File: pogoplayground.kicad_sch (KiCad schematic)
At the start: 48 parts, among them J2 Conn_01x20, J3 Conn_ARM_JTAG_SWD_10, J4 Conn_ARM_JTAG_SWD_10, J5 Conn_01x08, J6 Conn_01x30, J7 Conn_02x04_Odd_Even, J8 Conn_01x24, J9 Conn_01x02

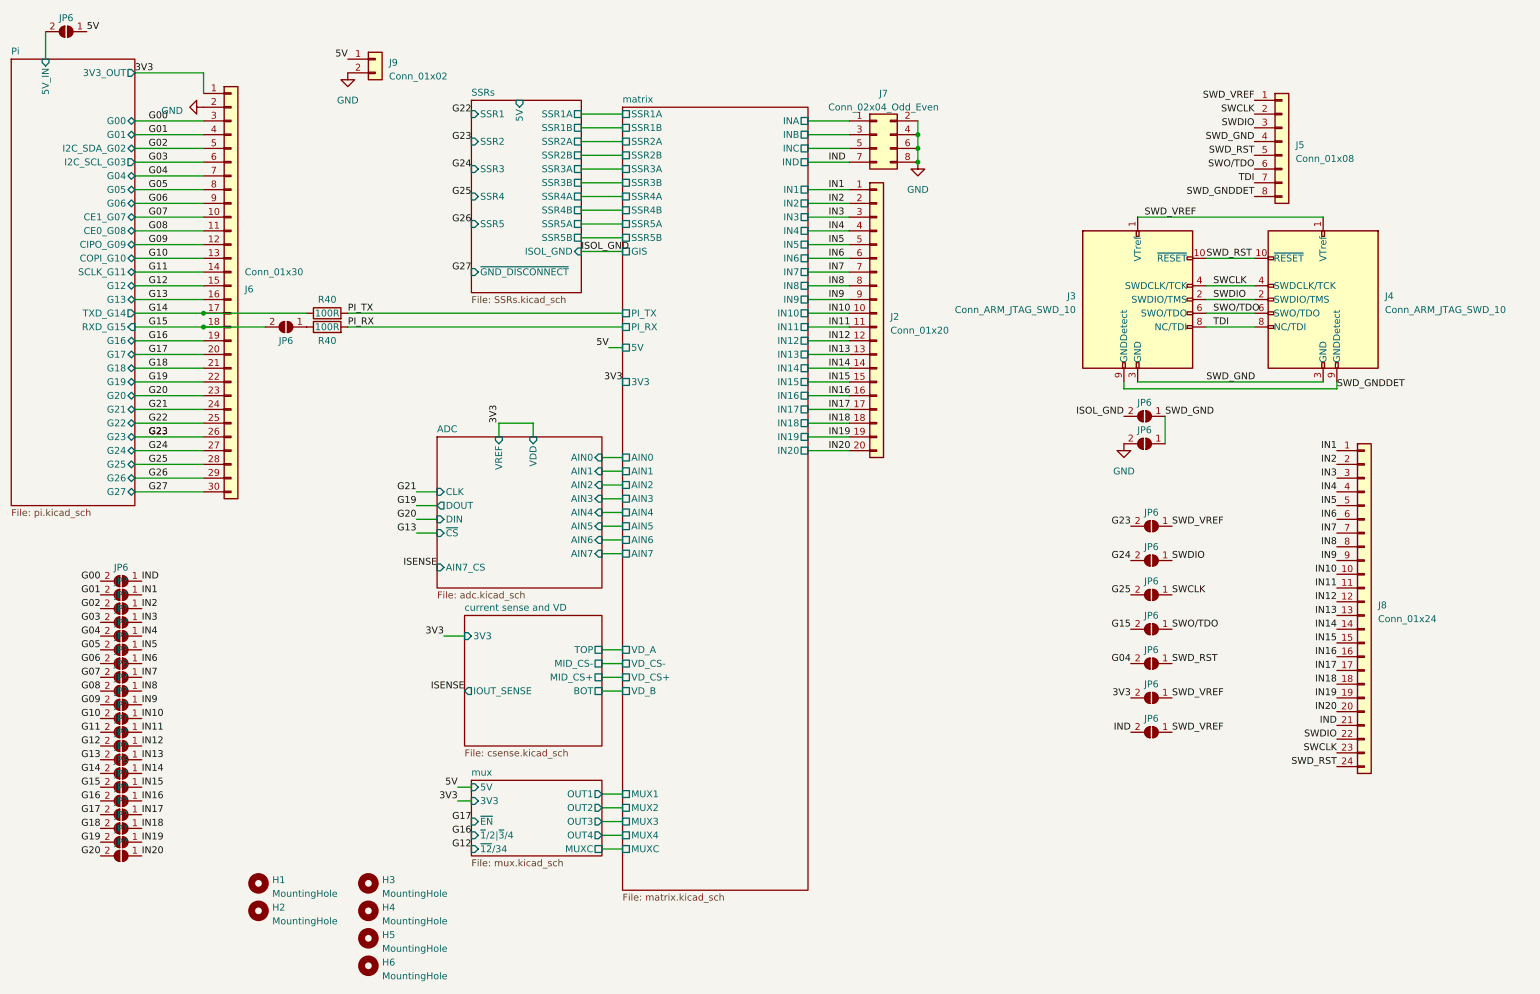
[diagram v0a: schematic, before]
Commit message: Build pogoplayground v1.0 - Fix continuity tester reference voltage - Fix SSR 5V supply
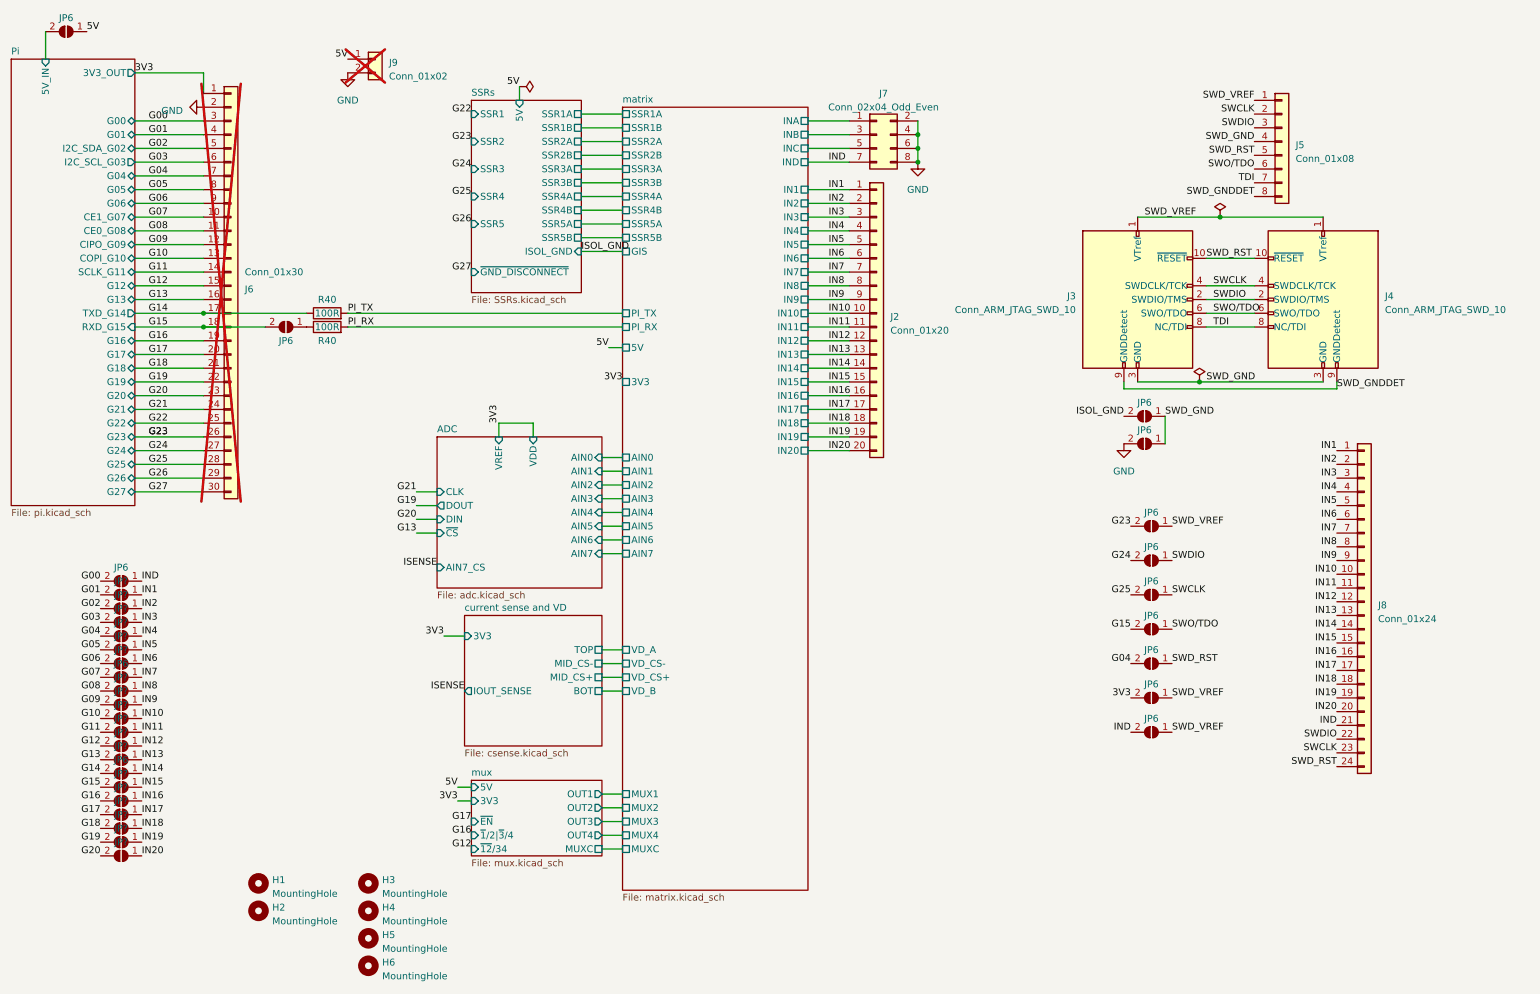
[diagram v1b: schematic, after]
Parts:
- J6, J9: now not fitted
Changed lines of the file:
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@@
   (junction (at 182.88 35.56) (diameter 0) (color 0 0 0 0)
   )
+  (junction (at 238.76 50.8) (diameter 0) (color 0 0 0 0)
+  )
   (junction (at 182.88 40.64) (diameter 0) (color 0 0 0 0)
   )
-  (wire (pts (xy 223.52 81.28) (xy 257.81 81.28))
+  (junction (at 234.95 81.28) (diameter 0) (color 0 0 0 0)
+  )
+  (wire (pts (xy 223.52 81.28) (xy 234.95 81.28))
     (stroke (width 0) (type default))
   )
@@
     (stroke (width 0) (type default))
   )
-  (wire (pts (xy 223.52 50.8) (xy 257.81 50.8))
+  (wire (pts (xy 223.52 50.8) (xy 238.76 50.8))
     (stroke (width 0) (type default))
   )
@@
     (stroke (width 0) (type default))
   )
+  (wire (pts (xy 234.95 81.28) (xy 257.81 81.28))
+    (stroke (width 0) (type default))
+  )
   (wire (pts (xy 38.1 88.9) (xy 50.8 88.9))
     (stroke (width 0) (type default))
@@
     (stroke (width 0) (type default))
   )
+  (wire (pts (xy 238.76 50.8) (xy 257.81 50.8))
+    (stroke (width 0) (type default))
+  )
   (wire (pts (xy 120.65 49.53) (xy 128.27 49.53))
     (stroke (width 0) (type default))
@@
     (stroke (width 0) (type default))
   )
+  (wire (pts (xy 109.22 26.67) (xy 109.22 29.21))
+    (stroke (width 0) (type default))
+  )
   (wire (pts (xy 162.56 40.64) (xy 170.18 40.64))
     (stroke (width 0) (type default))
@@
   )
   (label "G10" (at 31.75 143.51 180) (fields_autoplaced)
+    (effects (font (size 1.27 1.27)) (justify right bottom))
+  )
+  (label "5V" (at 109.22 26.67 180) (fields_autoplaced)
     (effects (font (size 1.27 1.27)) (justify right bottom))
   )
@@
   )
   (symbol (lib_id "Connector_Generic:Conn_01x02") (at 82.55 21.59 0) (unit 1)
-    (in_bom yes) (on_board yes) (dnp no) (fields_autoplaced)
+    (in_bom yes) (on_board yes) (dnp yes) (fields_autoplaced)
     (property "Reference" "J9" (at 85.09 22.225 0)
       (effects (font (size 1.27 1.27)) (justify left))
@@
   )
   (symbol (lib_id "Connector_Generic:Conn_01x30") (at 55.88 63.5 0) (unit 1)
-    (in_bom yes) (on_board yes) (dnp no)
+    (in_bom yes) (on_board yes) (dnp yes)
     (property "Reference" "J6" (at 58.42 64.135 0)
       (effects (font (size 1.27 1.27)) (justify left))
@@
     )
   )
+  (symbol (lib_id "power:PWR_FLAG") (at 234.95 81.28 0) (unit 1)
+    (in_bom yes) (on_board yes) (dnp no) (fields_autoplaced)
+    (property "Reference" "#FLG01" (at 234.95 79.375 0)
+      (effects (font (size 1.27 1.27)) hide)
+    )
+    (property "Value" "PWR_FLAG" (at 234.95 76.2 0)
+      (effects (font (size 1.27 1.27)) hide)
+    )
+    (property "Footprint" "" (at 234.95 81.28 0)
+      (effects (font (size 1.27 1.27)) hide)
+    )
+    (property "Datasheet" "~" (at 234.95 81.28 0)
+      (effects (font (size 1.27 1.27)) hide)
+    )
+    (pin "1")
+    (instances
+      (project "pogoplayground"
+        (path "/086fca78-0381-464b-8bbb-5a6257773e1c"
+          (reference "#FLG01") (unit 1)
+        )
+      )
+    )
+  )
   (symbol (lib_id "Jumper:SolderJumper_2_Open") (at 35.56 140.97 180) (unit 1)
     (in_bom yes) (on_board yes) (dnp no) (fields_autoplaced)
@@
     )
   )
+  (symbol (lib_id "power:PWR_FLAG") (at 238.76 50.8 0) (unit 1)
+    (in_bom yes) (on_board yes) (dnp no) (fields_autoplaced)
+    (property "Reference" "#FLG02" (at 238.76 48.895 0)
+      (effects (font (size 1.27 1.27)) hide)
+    )
+    (property "Value" "PWR_FLAG" (at 238.76 45.72 0)
+      (effects (font (size 1.27 1.27)) hide)
+    )
+    (property "Footprint" "" (at 238.76 50.8 0)
+      (effects (font (size 1.27 1.27)) hide)
+    )
+    (property "Datasheet" "~" (at 238.76 50.8 0)
+      (effects (font (size 1.27 1.27)) hide)
+    )
+    (pin "1")
+    (instances
+      (project "pogoplayground"
+        (path "/086fca78-0381-464b-8bbb-5a6257773e1c"
+          (reference "#FLG02") (unit 1)
+        )
+      )
+    )
+  )
   (symbol (lib_id "Jumper:SolderJumper_2_Open") (at 224.79 87.63 180) (unit 1)
     (in_bom yes) (on_board yes) (dnp no) (fields_autoplaced)
@@
         )
       )
+    )
+  )
+  (symbol (lib_id "power:PWR_FLAG") (at 109.22 26.67 270) (unit 1)
+    (in_bom yes) (on_board yes) (dnp no) (fields_autoplaced)
+    (property "Reference" "#FLG07" (at 111.125 26.67 0)
+      (effects (font (size 1.27 1.27)) hide)
+    )
+    (property "Value" "PWR_FLAG" (at 114.3 26.67 0)
+      (effects (font (size 1.27 1.27)) hide)
+    )
+    (property "Footprint" "" (at 109.22 26.67 0)
+      (effects (font (size 1.27 1.27)) hide)
+    )
+    (property "Datasheet" "~" (at 109.22 26.67 0)
+      (effects (font (size 1.27 1.27)) hide)
+    )
+    (pin "1")
+    (instances
+      (project "pogoplayground"
+        (path "/086fca78-0381-464b-8bbb-5a6257773e1c"
+          (reference "#FLG07") (unit 1)
+        )
+      )
